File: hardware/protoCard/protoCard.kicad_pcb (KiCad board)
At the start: 2 copper layers, 100 x 99.9 mm, 2 parts, among them J1 6502 Edge, J2 6502 Pinheader

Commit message: Protoboard v0.5
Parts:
- added REF**: TestPoint_THTPad_D1.5mm_Drill0.7mm, TestPoint:TestPoint_THTPad_D1.5mm_Drill0.7mm, F.Cu at (57.4, 34.6)
- added REF**1: TestPoint_THTPad_D1.5mm_Drill0.7mm, TestPoint:TestPoint_THTPad_D1.5mm_Drill0.7mm, F.Cu at (59.9, 34.6)
- added REF**10: TestPoint_THTPad_D1.5mm_Drill0.7mm, TestPoint:TestPoint_THTPad_D1.5mm_Drill0.7mm, F.Cu at (82.8, 34.6)
- added REF**100: TestPoint_THTPad_D1.5mm_Drill0.7mm, TestPoint:TestPoint_THTPad_D1.5mm_Drill0.7mm, F.Cu at (123.4, 39.7)
- added REF**1000: TestPoint_THTPad_D1.5mm_Drill0.7mm, TestPoint:TestPoint_THTPad_D1.5mm_Drill0.7mm, F.Cu at (59.9, 103.2)
- added REF**1001: TestPoint_THTPad_D1.5mm_Drill0.7mm, TestPoint:TestPoint_THTPad_D1.5mm_Drill0.7mm, F.Cu at (62.5, 103.2)
- added REF**1002: TestPoint_THTPad_D1.5mm_Drill0.7mm, TestPoint:TestPoint_THTPad_D1.5mm_Drill0.7mm, F.Cu at (65.0, 103.2)
- added REF**1003: TestPoint_THTPad_D1.5mm_Drill0.7mm, TestPoint:TestPoint_THTPad_D1.5mm_Drill0.7mm, F.Cu at (67.6, 103.2)
- added REF**1004: TestPoint_THTPad_D1.5mm_Drill0.7mm, TestPoint:TestPoint_THTPad_D1.5mm_Drill0.7mm, F.Cu at (70.1, 103.2)
- added REF**1005: TestPoint_THTPad_D1.5mm_Drill0.7mm, TestPoint:TestPoint_THTPad_D1.5mm_Drill0.7mm, F.Cu at (72.6, 103.2)
- added REF**1006: TestPoint_THTPad_D1.5mm_Drill0.7mm, TestPoint:TestPoint_THTPad_D1.5mm_Drill0.7mm, F.Cu at (75.2, 103.2)
- added REF**1007: TestPoint_THTPad_D1.5mm_Drill0.7mm, TestPoint:TestPoint_THTPad_D1.5mm_Drill0.7mm, F.Cu at (77.7, 103.2)
- added REF**1008: TestPoint_THTPad_D1.5mm_Drill0.7mm, TestPoint:TestPoint_THTPad_D1.5mm_Drill0.7mm, F.Cu at (80.3, 103.2)
- added REF**1009: TestPoint_THTPad_D1.5mm_Drill0.7mm, TestPoint:TestPoint_THTPad_D1.5mm_Drill0.7mm, F.Cu at (82.8, 103.2)
- added REF**101: TestPoint_THTPad_D1.5mm_Drill0.7mm, TestPoint:TestPoint_THTPad_D1.5mm_Drill0.7mm, F.Cu at (126.0, 39.7)
- added REF**1010: TestPoint_THTPad_D1.5mm_Drill0.7mm, TestPoint:TestPoint_THTPad_D1.5mm_Drill0.7mm, F.Cu at (85.3, 103.2)
- added REF**1011: TestPoint_THTPad_D1.5mm_Drill0.7mm, TestPoint:TestPoint_THTPad_D1.5mm_Drill0.7mm, F.Cu at (87.9, 103.2)
- added REF**1012: TestPoint_THTPad_D1.5mm_Drill0.7mm, TestPoint:TestPoint_THTPad_D1.5mm_Drill0.7mm, F.Cu at (90.4, 103.2)
- added REF**1013: TestPoint_THTPad_D1.5mm_Drill0.7mm, TestPoint:TestPoint_THTPad_D1.5mm_Drill0.7mm, F.Cu at (93.0, 103.2)
- added REF**1014: TestPoint_THTPad_D1.5mm_Drill0.7mm, TestPoint:TestPoint_THTPad_D1.5mm_Drill0.7mm, F.Cu at (95.5, 103.2)
- added REF**1015: TestPoint_THTPad_D1.5mm_Drill0.7mm, TestPoint:TestPoint_THTPad_D1.5mm_Drill0.7mm, F.Cu at (98.0, 103.2)
- added REF**1016: TestPoint_THTPad_D1.5mm_Drill0.7mm, TestPoint:TestPoint_THTPad_D1.5mm_Drill0.7mm, F.Cu at (100.6, 103.2)
- added REF**1017: TestPoint_THTPad_D1.5mm_Drill0.7mm, TestPoint:TestPoint_THTPad_D1.5mm_Drill0.7mm, F.Cu at (103.1, 103.2)
- added REF**1018: TestPoint_THTPad_D1.5mm_Drill0.7mm, TestPoint:TestPoint_THTPad_D1.5mm_Drill0.7mm, F.Cu at (105.7, 103.2)
- added REF**1019: TestPoint_THTPad_D1.5mm_Drill0.7mm, TestPoint:TestPoint_THTPad_D1.5mm_Drill0.7mm, F.Cu at (108.2, 103.2)
- added REF**102: TestPoint_THTPad_D1.5mm_Drill0.7mm, TestPoint:TestPoint_THTPad_D1.5mm_Drill0.7mm, F.Cu at (128.5, 39.7)
- added REF**1020: TestPoint_THTPad_D1.5mm_Drill0.7mm, TestPoint:TestPoint_THTPad_D1.5mm_Drill0.7mm, F.Cu at (110.7, 103.2)
- added REF**1021: TestPoint_THTPad_D1.5mm_Drill0.7mm, TestPoint:TestPoint_THTPad_D1.5mm_Drill0.7mm, F.Cu at (113.3, 103.2)
- added REF**1022: TestPoint_THTPad_D1.5mm_Drill0.7mm, TestPoint:TestPoint_THTPad_D1.5mm_Drill0.7mm, F.Cu at (115.8, 103.2)
- added REF**1023: TestPoint_THTPad_D1.5mm_Drill0.7mm, TestPoint:TestPoint_THTPad_D1.5mm_Drill0.7mm, F.Cu at (118.4, 103.2)
- added REF**1024: TestPoint_THTPad_D1.5mm_Drill0.7mm, TestPoint:TestPoint_THTPad_D1.5mm_Drill0.7mm, F.Cu at (120.9, 103.2)
- added REF**1025: TestPoint_THTPad_D1.5mm_Drill0.7mm, TestPoint:TestPoint_THTPad_D1.5mm_Drill0.7mm, F.Cu at (123.4, 103.2)
- added REF**1026: TestPoint_THTPad_D1.5mm_Drill0.7mm, TestPoint:TestPoint_THTPad_D1.5mm_Drill0.7mm, F.Cu at (126.0, 103.2)
- added REF**1027: TestPoint_THTPad_D1.5mm_Drill0.7mm, TestPoint:TestPoint_THTPad_D1.5mm_Drill0.7mm, F.Cu at (128.5, 103.2)
- added REF**1028: TestPoint_THTPad_D1.5mm_Drill0.7mm, TestPoint:TestPoint_THTPad_D1.5mm_Drill0.7mm, F.Cu at (131.1, 103.2)
- added REF**1029: TestPoint_THTPad_D1.5mm_Drill0.7mm, TestPoint:TestPoint_THTPad_D1.5mm_Drill0.7mm, F.Cu at (133.6, 103.2)
- added REF**103: TestPoint_THTPad_D1.5mm_Drill0.7mm, TestPoint:TestPoint_THTPad_D1.5mm_Drill0.7mm, F.Cu at (131.1, 39.7)
- added REF**1030: TestPoint_THTPad_D1.5mm_Drill0.7mm, TestPoint:TestPoint_THTPad_D1.5mm_Drill0.7mm, F.Cu at (136.1, 103.2)
- added REF**1031: TestPoint_THTPad_D1.5mm_Drill0.7mm, TestPoint:TestPoint_THTPad_D1.5mm_Drill0.7mm, F.Cu at (138.7, 103.2)
- added REF**1032: TestPoint_THTPad_D1.5mm_Drill0.7mm, TestPoint:TestPoint_THTPad_D1.5mm_Drill0.7mm, F.Cu at (141.2, 103.2)
- added REF**1033: TestPoint_THTPad_D1.5mm_Drill0.7mm, TestPoint:TestPoint_THTPad_D1.5mm_Drill0.7mm, F.Cu at (143.8, 103.2)
- added REF**1034: TestPoint_THTPad_D1.5mm_Drill0.7mm, TestPoint:TestPoint_THTPad_D1.5mm_Drill0.7mm, F.Cu at (146.3, 103.2)
- added REF**1035: TestPoint_THTPad_D1.5mm_Drill0.7mm, TestPoint:TestPoint_THTPad_D1.5mm_Drill0.7mm, F.Cu at (148.8, 103.2)
- added REF**1037: TestPoint_THTPad_D1.5mm_Drill0.7mm, TestPoint:TestPoint_THTPad_D1.5mm_Drill0.7mm, F.Cu at (59.9, 105.7)
- added REF**1038: TestPoint_THTPad_D1.5mm_Drill0.7mm, TestPoint:TestPoint_THTPad_D1.5mm_Drill0.7mm, F.Cu at (62.5, 105.7)
- added REF**1039: TestPoint_THTPad_D1.5mm_Drill0.7mm, TestPoint:TestPoint_THTPad_D1.5mm_Drill0.7mm, F.Cu at (65.0, 105.7)
- added REF**104: TestPoint_THTPad_D1.5mm_Drill0.7mm, TestPoint:TestPoint_THTPad_D1.5mm_Drill0.7mm, F.Cu at (133.6, 39.7)
- added REF**1040: TestPoint_THTPad_D1.5mm_Drill0.7mm, TestPoint:TestPoint_THTPad_D1.5mm_Drill0.7mm, F.Cu at (67.6, 105.7)
- added REF**1041: TestPoint_THTPad_D1.5mm_Drill0.7mm, TestPoint:TestPoint_THTPad_D1.5mm_Drill0.7mm, F.Cu at (70.1, 105.7)
- added REF**1042: TestPoint_THTPad_D1.5mm_Drill0.7mm, TestPoint:TestPoint_THTPad_D1.5mm_Drill0.7mm, F.Cu at (72.6, 105.7)
- added REF**1043: TestPoint_THTPad_D1.5mm_Drill0.7mm, TestPoint:TestPoint_THTPad_D1.5mm_Drill0.7mm, F.Cu at (75.2, 105.7)
- added REF**1044: TestPoint_THTPad_D1.5mm_Drill0.7mm, TestPoint:TestPoint_THTPad_D1.5mm_Drill0.7mm, F.Cu at (77.7, 105.7)
- added REF**1045: TestPoint_THTPad_D1.5mm_Drill0.7mm, TestPoint:TestPoint_THTPad_D1.5mm_Drill0.7mm, F.Cu at (80.3, 105.7)
- added REF**1046: TestPoint_THTPad_D1.5mm_Drill0.7mm, TestPoint:TestPoint_THTPad_D1.5mm_Drill0.7mm, F.Cu at (82.8, 105.7)
- added REF**1047: TestPoint_THTPad_D1.5mm_Drill0.7mm, TestPoint:TestPoint_THTPad_D1.5mm_Drill0.7mm, F.Cu at (85.3, 105.7)
- added REF**1048: TestPoint_THTPad_D1.5mm_Drill0.7mm, TestPoint:TestPoint_THTPad_D1.5mm_Drill0.7mm, F.Cu at (87.9, 105.7)
- added REF**1049: TestPoint_THTPad_D1.5mm_Drill0.7mm, TestPoint:TestPoint_THTPad_D1.5mm_Drill0.7mm, F.Cu at (90.4, 105.7)
- added REF**105: TestPoint_THTPad_D1.5mm_Drill0.7mm, TestPoint:TestPoint_THTPad_D1.5mm_Drill0.7mm, F.Cu at (136.1, 39.7)
- added REF**1050: TestPoint_THTPad_D1.5mm_Drill0.7mm, TestPoint:TestPoint_THTPad_D1.5mm_Drill0.7mm, F.Cu at (93.0, 105.7)
- added REF**1051: TestPoint_THTPad_D1.5mm_Drill0.7mm, TestPoint:TestPoint_THTPad_D1.5mm_Drill0.7mm, F.Cu at (95.5, 105.7)
- added REF**1052: TestPoint_THTPad_D1.5mm_Drill0.7mm, TestPoint:TestPoint_THTPad_D1.5mm_Drill0.7mm, F.Cu at (98.0, 105.7)
- added REF**1053: TestPoint_THTPad_D1.5mm_Drill0.7mm, TestPoint:TestPoint_THTPad_D1.5mm_Drill0.7mm, F.Cu at (100.6, 105.7)
- added REF**1054: TestPoint_THTPad_D1.5mm_Drill0.7mm, TestPoint:TestPoint_THTPad_D1.5mm_Drill0.7mm, F.Cu at (103.1, 105.7)
- added REF**1055: TestPoint_THTPad_D1.5mm_Drill0.7mm, TestPoint:TestPoint_THTPad_D1.5mm_Drill0.7mm, F.Cu at (105.7, 105.7)
- added REF**1056: TestPoint_THTPad_D1.5mm_Drill0.7mm, TestPoint:TestPoint_THTPad_D1.5mm_Drill0.7mm, F.Cu at (108.2, 105.7)
- added REF**1057: TestPoint_THTPad_D1.5mm_Drill0.7mm, TestPoint:TestPoint_THTPad_D1.5mm_Drill0.7mm, F.Cu at (110.7, 105.7)
- added REF**1058: TestPoint_THTPad_D1.5mm_Drill0.7mm, TestPoint:TestPoint_THTPad_D1.5mm_Drill0.7mm, F.Cu at (113.3, 105.7)
- added REF**1059: TestPoint_THTPad_D1.5mm_Drill0.7mm, TestPoint:TestPoint_THTPad_D1.5mm_Drill0.7mm, F.Cu at (115.8, 105.7)
- added REF**106: TestPoint_THTPad_D1.5mm_Drill0.7mm, TestPoint:TestPoint_THTPad_D1.5mm_Drill0.7mm, F.Cu at (138.7, 39.7)
- added REF**1060: TestPoint_THTPad_D1.5mm_Drill0.7mm, TestPoint:TestPoint_THTPad_D1.5mm_Drill0.7mm, F.Cu at (118.4, 105.7)
- added REF**1061: TestPoint_THTPad_D1.5mm_Drill0.7mm, TestPoint:TestPoint_THTPad_D1.5mm_Drill0.7mm, F.Cu at (120.9, 105.7)
- added REF**1062: TestPoint_THTPad_D1.5mm_Drill0.7mm, TestPoint:TestPoint_THTPad_D1.5mm_Drill0.7mm, F.Cu at (123.4, 105.7)
- added REF**1063: TestPoint_THTPad_D1.5mm_Drill0.7mm, TestPoint:TestPoint_THTPad_D1.5mm_Drill0.7mm, F.Cu at (126.0, 105.7)
- added REF**1064: TestPoint_THTPad_D1.5mm_Drill0.7mm, TestPoint:TestPoint_THTPad_D1.5mm_Drill0.7mm, F.Cu at (128.5, 105.7)
- added REF**1065: TestPoint_THTPad_D1.5mm_Drill0.7mm, TestPoint:TestPoint_THTPad_D1.5mm_Drill0.7mm, F.Cu at (131.1, 105.7)
- added REF**1066: TestPoint_THTPad_D1.5mm_Drill0.7mm, TestPoint:TestPoint_THTPad_D1.5mm_Drill0.7mm, F.Cu at (133.6, 105.7)
- added REF**1067: TestPoint_THTPad_D1.5mm_Drill0.7mm, TestPoint:TestPoint_THTPad_D1.5mm_Drill0.7mm, F.Cu at (136.1, 105.7)
- added REF**1068: TestPoint_THTPad_D1.5mm_Drill0.7mm, TestPoint:TestPoint_THTPad_D1.5mm_Drill0.7mm, F.Cu at (138.7, 105.7)
- added REF**1069: TestPoint_THTPad_D1.5mm_Drill0.7mm, TestPoint:TestPoint_THTPad_D1.5mm_Drill0.7mm, F.Cu at (141.2, 105.7)
- added REF**107: TestPoint_THTPad_D1.5mm_Drill0.7mm, TestPoint:TestPoint_THTPad_D1.5mm_Drill0.7mm, F.Cu at (141.2, 39.7)
- added REF**1070: TestPoint_THTPad_D1.5mm_Drill0.7mm, TestPoint:TestPoint_THTPad_D1.5mm_Drill0.7mm, F.Cu at (143.8, 105.7)
- added REF**1071: TestPoint_THTPad_D1.5mm_Drill0.7mm, TestPoint:TestPoint_THTPad_D1.5mm_Drill0.7mm, F.Cu at (146.3, 105.7)
- added REF**1072: TestPoint_THTPad_D1.5mm_Drill0.7mm, TestPoint:TestPoint_THTPad_D1.5mm_Drill0.7mm, F.Cu at (148.8, 105.7)
- added REF**108: TestPoint_THTPad_D1.5mm_Drill0.7mm, TestPoint:TestPoint_THTPad_D1.5mm_Drill0.7mm, F.Cu at (143.8, 39.7)
- added REF**109: TestPoint_THTPad_D1.5mm_Drill0.7mm, TestPoint:TestPoint_THTPad_D1.5mm_Drill0.7mm, F.Cu at (148.8, 39.7)
- added REF**11: TestPoint_THTPad_D1.5mm_Drill0.7mm, TestPoint:TestPoint_THTPad_D1.5mm_Drill0.7mm, F.Cu at (85.3, 34.6)
- added REF**110: TestPoint_THTPad_D1.5mm_Drill0.7mm, TestPoint:TestPoint_THTPad_D1.5mm_Drill0.7mm, F.Cu at (148.8, 42.2)
- added REF**111: TestPoint_THTPad_D1.5mm_Drill0.7mm, TestPoint:TestPoint_THTPad_D1.5mm_Drill0.7mm, F.Cu at (57.4, 42.2)
- added REF**112: TestPoint_THTPad_D1.5mm_Drill0.7mm, TestPoint:TestPoint_THTPad_D1.5mm_Drill0.7mm, F.Cu at (59.9, 42.2)
- added REF**113: TestPoint_THTPad_D1.5mm_Drill0.7mm, TestPoint:TestPoint_THTPad_D1.5mm_Drill0.7mm, F.Cu at (62.5, 42.2)
- added REF**114: TestPoint_THTPad_D1.5mm_Drill0.7mm, TestPoint:TestPoint_THTPad_D1.5mm_Drill0.7mm, F.Cu at (65.0, 42.2)
- added REF**115: TestPoint_THTPad_D1.5mm_Drill0.7mm, TestPoint:TestPoint_THTPad_D1.5mm_Drill0.7mm, F.Cu at (67.6, 42.2)
- added REF**116: TestPoint_THTPad_D1.5mm_Drill0.7mm, TestPoint:TestPoint_THTPad_D1.5mm_Drill0.7mm, F.Cu at (70.1, 42.2)
- added REF**117: TestPoint_THTPad_D1.5mm_Drill0.7mm, TestPoint:TestPoint_THTPad_D1.5mm_Drill0.7mm, F.Cu at (72.6, 42.2)
- added REF**118: TestPoint_THTPad_D1.5mm_Drill0.7mm, TestPoint:TestPoint_THTPad_D1.5mm_Drill0.7mm, F.Cu at (75.2, 42.2)
- added REF**119: TestPoint_THTPad_D1.5mm_Drill0.7mm, TestPoint:TestPoint_THTPad_D1.5mm_Drill0.7mm, F.Cu at (77.7, 42.2)
- added REF**12: TestPoint_THTPad_D1.5mm_Drill0.7mm, TestPoint:TestPoint_THTPad_D1.5mm_Drill0.7mm, F.Cu at (87.9, 34.6)
- added REF**120: TestPoint_THTPad_D1.5mm_Drill0.7mm, TestPoint:TestPoint_THTPad_D1.5mm_Drill0.7mm, F.Cu at (80.3, 42.2)
- added REF**121: TestPoint_THTPad_D1.5mm_Drill0.7mm, TestPoint:TestPoint_THTPad_D1.5mm_Drill0.7mm, F.Cu at (82.8, 42.2)
- added REF**122: TestPoint_THTPad_D1.5mm_Drill0.7mm, TestPoint:TestPoint_THTPad_D1.5mm_Drill0.7mm, F.Cu at (85.3, 42.2)
- added REF**123: TestPoint_THTPad_D1.5mm_Drill0.7mm, TestPoint:TestPoint_THTPad_D1.5mm_Drill0.7mm, F.Cu at (87.9, 42.2)
- added REF**124: TestPoint_THTPad_D1.5mm_Drill0.7mm, TestPoint:TestPoint_THTPad_D1.5mm_Drill0.7mm, F.Cu at (90.4, 42.2)
- added REF**125: TestPoint_THTPad_D1.5mm_Drill0.7mm, TestPoint:TestPoint_THTPad_D1.5mm_Drill0.7mm, F.Cu at (93.0, 42.2)
- added REF**126: TestPoint_THTPad_D1.5mm_Drill0.7mm, TestPoint:TestPoint_THTPad_D1.5mm_Drill0.7mm, F.Cu at (95.5, 42.2)
- added REF**127: TestPoint_THTPad_D1.5mm_Drill0.7mm, TestPoint:TestPoint_THTPad_D1.5mm_Drill0.7mm, F.Cu at (98.0, 42.2)
- added REF**128: TestPoint_THTPad_D1.5mm_Drill0.7mm, TestPoint:TestPoint_THTPad_D1.5mm_Drill0.7mm, F.Cu at (100.6, 42.2)
- added REF**129: TestPoint_THTPad_D1.5mm_Drill0.7mm, TestPoint:TestPoint_THTPad_D1.5mm_Drill0.7mm, F.Cu at (103.1, 42.2)
- added REF**13: TestPoint_THTPad_D1.5mm_Drill0.7mm, TestPoint:TestPoint_THTPad_D1.5mm_Drill0.7mm, F.Cu at (90.4, 34.6)
- added REF**130: TestPoint_THTPad_D1.5mm_Drill0.7mm, TestPoint:TestPoint_THTPad_D1.5mm_Drill0.7mm, F.Cu at (105.7, 42.2)
- added REF**131: TestPoint_THTPad_D1.5mm_Drill0.7mm, TestPoint:TestPoint_THTPad_D1.5mm_Drill0.7mm, F.Cu at (108.2, 42.2)
- added REF**132: TestPoint_THTPad_D1.5mm_Drill0.7mm, TestPoint:TestPoint_THTPad_D1.5mm_Drill0.7mm, F.Cu at (110.7, 42.2)
- added REF**133: TestPoint_THTPad_D1.5mm_Drill0.7mm, TestPoint:TestPoint_THTPad_D1.5mm_Drill0.7mm, F.Cu at (113.3, 42.2)
- added REF**134: TestPoint_THTPad_D1.5mm_Drill0.7mm, TestPoint:TestPoint_THTPad_D1.5mm_Drill0.7mm, F.Cu at (115.8, 42.2)
- added REF**135: TestPoint_THTPad_D1.5mm_Drill0.7mm, TestPoint:TestPoint_THTPad_D1.5mm_Drill0.7mm, F.Cu at (118.4, 42.2)
- added REF**136: TestPoint_THTPad_D1.5mm_Drill0.7mm, TestPoint:TestPoint_THTPad_D1.5mm_Drill0.7mm, F.Cu at (120.9, 42.2)
- added REF**137: TestPoint_THTPad_D1.5mm_Drill0.7mm, TestPoint:TestPoint_THTPad_D1.5mm_Drill0.7mm, F.Cu at (123.4, 42.2)
- added REF**138: TestPoint_THTPad_D1.5mm_Drill0.7mm, TestPoint:TestPoint_THTPad_D1.5mm_Drill0.7mm, F.Cu at (126.0, 42.2)
- added REF**139: TestPoint_THTPad_D1.5mm_Drill0.7mm, TestPoint:TestPoint_THTPad_D1.5mm_Drill0.7mm, F.Cu at (128.5, 42.2)
- added REF**14: TestPoint_THTPad_D1.5mm_Drill0.7mm, TestPoint:TestPoint_THTPad_D1.5mm_Drill0.7mm, F.Cu at (93.0, 34.6)
- added REF**140: TestPoint_THTPad_D1.5mm_Drill0.7mm, TestPoint:TestPoint_THTPad_D1.5mm_Drill0.7mm, F.Cu at (131.1, 42.2)
- added REF**141: TestPoint_THTPad_D1.5mm_Drill0.7mm, TestPoint:TestPoint_THTPad_D1.5mm_Drill0.7mm, F.Cu at (133.6, 42.2)
- added REF**142: TestPoint_THTPad_D1.5mm_Drill0.7mm, TestPoint:TestPoint_THTPad_D1.5mm_Drill0.7mm, F.Cu at (136.1, 42.2)
- added REF**143: TestPoint_THTPad_D1.5mm_Drill0.7mm, TestPoint:TestPoint_THTPad_D1.5mm_Drill0.7mm, F.Cu at (138.7, 42.2)
- added REF**144: TestPoint_THTPad_D1.5mm_Drill0.7mm, TestPoint:TestPoint_THTPad_D1.5mm_Drill0.7mm, F.Cu at (141.2, 42.2)
- added REF**145: TestPoint_THTPad_D1.5mm_Drill0.7mm, TestPoint:TestPoint_THTPad_D1.5mm_Drill0.7mm, F.Cu at (143.8, 42.2)
- added REF**146: TestPoint_THTPad_D1.5mm_Drill0.7mm, TestPoint:TestPoint_THTPad_D1.5mm_Drill0.7mm, F.Cu at (148.8, 44.8)
- added REF**147: TestPoint_THTPad_D1.5mm_Drill0.7mm, TestPoint:TestPoint_THTPad_D1.5mm_Drill0.7mm, F.Cu at (148.8, 47.3)
- added REF**148: TestPoint_THTPad_D1.5mm_Drill0.7mm, TestPoint:TestPoint_THTPad_D1.5mm_Drill0.7mm, F.Cu at (57.4, 44.8)
- added REF**149: TestPoint_THTPad_D1.5mm_Drill0.7mm, TestPoint:TestPoint_THTPad_D1.5mm_Drill0.7mm, F.Cu at (59.9, 44.8)
- added REF**15: TestPoint_THTPad_D1.5mm_Drill0.7mm, TestPoint:TestPoint_THTPad_D1.5mm_Drill0.7mm, F.Cu at (95.5, 34.6)
- added REF**150: TestPoint_THTPad_D1.5mm_Drill0.7mm, TestPoint:TestPoint_THTPad_D1.5mm_Drill0.7mm, F.Cu at (62.5, 44.8)
- added REF**151: TestPoint_THTPad_D1.5mm_Drill0.7mm, TestPoint:TestPoint_THTPad_D1.5mm_Drill0.7mm, F.Cu at (65.0, 44.8)
- added REF**152: TestPoint_THTPad_D1.5mm_Drill0.7mm, TestPoint:TestPoint_THTPad_D1.5mm_Drill0.7mm, F.Cu at (67.6, 44.8)
- added REF**153: TestPoint_THTPad_D1.5mm_Drill0.7mm, TestPoint:TestPoint_THTPad_D1.5mm_Drill0.7mm, F.Cu at (70.1, 44.8)
- added REF**154: TestPoint_THTPad_D1.5mm_Drill0.7mm, TestPoint:TestPoint_THTPad_D1.5mm_Drill0.7mm, F.Cu at (72.6, 44.8)
- added REF**155: TestPoint_THTPad_D1.5mm_Drill0.7mm, TestPoint:TestPoint_THTPad_D1.5mm_Drill0.7mm, F.Cu at (75.2, 44.8)
- added REF**156: TestPoint_THTPad_D1.5mm_Drill0.7mm, TestPoint:TestPoint_THTPad_D1.5mm_Drill0.7mm, F.Cu at (77.7, 44.8)
- added REF**157: TestPoint_THTPad_D1.5mm_Drill0.7mm, TestPoint:TestPoint_THTPad_D1.5mm_Drill0.7mm, F.Cu at (80.3, 44.8)
- added REF**158: TestPoint_THTPad_D1.5mm_Drill0.7mm, TestPoint:TestPoint_THTPad_D1.5mm_Drill0.7mm, F.Cu at (82.8, 44.8)
- added REF**159: TestPoint_THTPad_D1.5mm_Drill0.7mm, TestPoint:TestPoint_THTPad_D1.5mm_Drill0.7mm, F.Cu at (85.3, 44.8)
- added REF**16: TestPoint_THTPad_D1.5mm_Drill0.7mm, TestPoint:TestPoint_THTPad_D1.5mm_Drill0.7mm, F.Cu at (98.0, 34.6)
- added REF**160: TestPoint_THTPad_D1.5mm_Drill0.7mm, TestPoint:TestPoint_THTPad_D1.5mm_Drill0.7mm, F.Cu at (87.9, 44.8)
- added REF**161: TestPoint_THTPad_D1.5mm_Drill0.7mm, TestPoint:TestPoint_THTPad_D1.5mm_Drill0.7mm, F.Cu at (90.4, 44.8)
- added REF**162: TestPoint_THTPad_D1.5mm_Drill0.7mm, TestPoint:TestPoint_THTPad_D1.5mm_Drill0.7mm, F.Cu at (93.0, 44.8)
- added REF**163: TestPoint_THTPad_D1.5mm_Drill0.7mm, TestPoint:TestPoint_THTPad_D1.5mm_Drill0.7mm, F.Cu at (95.5, 44.8)
- added REF**164: TestPoint_THTPad_D1.5mm_Drill0.7mm, TestPoint:TestPoint_THTPad_D1.5mm_Drill0.7mm, F.Cu at (98.0, 44.8)
- added REF**165: TestPoint_THTPad_D1.5mm_Drill0.7mm, TestPoint:TestPoint_THTPad_D1.5mm_Drill0.7mm, F.Cu at (100.6, 44.8)
- added REF**166: TestPoint_THTPad_D1.5mm_Drill0.7mm, TestPoint:TestPoint_THTPad_D1.5mm_Drill0.7mm, F.Cu at (103.1, 44.8)
- added REF**167: TestPoint_THTPad_D1.5mm_Drill0.7mm, TestPoint:TestPoint_THTPad_D1.5mm_Drill0.7mm, F.Cu at (105.7, 44.8)
- added REF**168: TestPoint_THTPad_D1.5mm_Drill0.7mm, TestPoint:TestPoint_THTPad_D1.5mm_Drill0.7mm, F.Cu at (108.2, 44.8)
- added REF**169: TestPoint_THTPad_D1.5mm_Drill0.7mm, TestPoint:TestPoint_THTPad_D1.5mm_Drill0.7mm, F.Cu at (110.7, 44.8)
- added REF**17: TestPoint_THTPad_D1.5mm_Drill0.7mm, TestPoint:TestPoint_THTPad_D1.5mm_Drill0.7mm, F.Cu at (100.6, 34.6)
- added REF**170: TestPoint_THTPad_D1.5mm_Drill0.7mm, TestPoint:TestPoint_THTPad_D1.5mm_Drill0.7mm, F.Cu at (113.3, 44.8)
- added REF**171: TestPoint_THTPad_D1.5mm_Drill0.7mm, TestPoint:TestPoint_THTPad_D1.5mm_Drill0.7mm, F.Cu at (115.8, 44.8)
- added REF**172: TestPoint_THTPad_D1.5mm_Drill0.7mm, TestPoint:TestPoint_THTPad_D1.5mm_Drill0.7mm, F.Cu at (118.4, 44.8)
- added REF**173: TestPoint_THTPad_D1.5mm_Drill0.7mm, TestPoint:TestPoint_THTPad_D1.5mm_Drill0.7mm, F.Cu at (120.9, 44.8)
- added REF**174: TestPoint_THTPad_D1.5mm_Drill0.7mm, TestPoint:TestPoint_THTPad_D1.5mm_Drill0.7mm, F.Cu at (123.4, 44.8)
- added REF**175: TestPoint_THTPad_D1.5mm_Drill0.7mm, TestPoint:TestPoint_THTPad_D1.5mm_Drill0.7mm, F.Cu at (126.0, 44.8)
- added REF**176: TestPoint_THTPad_D1.5mm_Drill0.7mm, TestPoint:TestPoint_THTPad_D1.5mm_Drill0.7mm, F.Cu at (128.5, 44.8)
- added REF**177: TestPoint_THTPad_D1.5mm_Drill0.7mm, TestPoint:TestPoint_THTPad_D1.5mm_Drill0.7mm, F.Cu at (131.1, 44.8)
- added REF**178: TestPoint_THTPad_D1.5mm_Drill0.7mm, TestPoint:TestPoint_THTPad_D1.5mm_Drill0.7mm, F.Cu at (133.6, 44.8)
- added REF**179: TestPoint_THTPad_D1.5mm_Drill0.7mm, TestPoint:TestPoint_THTPad_D1.5mm_Drill0.7mm, F.Cu at (136.1, 44.8)
- added REF**18: TestPoint_THTPad_D1.5mm_Drill0.7mm, TestPoint:TestPoint_THTPad_D1.5mm_Drill0.7mm, F.Cu at (103.1, 34.6)
- added REF**180: TestPoint_THTPad_D1.5mm_Drill0.7mm, TestPoint:TestPoint_THTPad_D1.5mm_Drill0.7mm, F.Cu at (138.7, 44.8)
- added REF**181: TestPoint_THTPad_D1.5mm_Drill0.7mm, TestPoint:TestPoint_THTPad_D1.5mm_Drill0.7mm, F.Cu at (141.2, 44.8)
- added REF**182: TestPoint_THTPad_D1.5mm_Drill0.7mm, TestPoint:TestPoint_THTPad_D1.5mm_Drill0.7mm, F.Cu at (143.8, 44.8)
- added REF**183: TestPoint_THTPad_D1.5mm_Drill0.7mm, TestPoint:TestPoint_THTPad_D1.5mm_Drill0.7mm, F.Cu at (148.8, 49.8)
- added REF**184: TestPoint_THTPad_D1.5mm_Drill0.7mm, TestPoint:TestPoint_THTPad_D1.5mm_Drill0.7mm, F.Cu at (148.8, 52.4)
- added REF**185: TestPoint_THTPad_D1.5mm_Drill0.7mm, TestPoint:TestPoint_THTPad_D1.5mm_Drill0.7mm, F.Cu at (57.4, 47.3)
- added REF**186: TestPoint_THTPad_D1.5mm_Drill0.7mm, TestPoint:TestPoint_THTPad_D1.5mm_Drill0.7mm, F.Cu at (59.9, 47.3)
- added REF**187: TestPoint_THTPad_D1.5mm_Drill0.7mm, TestPoint:TestPoint_THTPad_D1.5mm_Drill0.7mm, F.Cu at (62.5, 47.3)
- added REF**188: TestPoint_THTPad_D1.5mm_Drill0.7mm, TestPoint:TestPoint_THTPad_D1.5mm_Drill0.7mm, F.Cu at (65.0, 47.3)
- added REF**189: TestPoint_THTPad_D1.5mm_Drill0.7mm, TestPoint:TestPoint_THTPad_D1.5mm_Drill0.7mm, F.Cu at (67.6, 47.3)
- added REF**19: TestPoint_THTPad_D1.5mm_Drill0.7mm, TestPoint:TestPoint_THTPad_D1.5mm_Drill0.7mm, F.Cu at (105.7, 34.6)
- added REF**190: TestPoint_THTPad_D1.5mm_Drill0.7mm, TestPoint:TestPoint_THTPad_D1.5mm_Drill0.7mm, F.Cu at (70.1, 47.3)
- added REF**191: TestPoint_THTPad_D1.5mm_Drill0.7mm, TestPoint:TestPoint_THTPad_D1.5mm_Drill0.7mm, F.Cu at (72.6, 47.3)
- added REF**192: TestPoint_THTPad_D1.5mm_Drill0.7mm, TestPoint:TestPoint_THTPad_D1.5mm_Drill0.7mm, F.Cu at (75.2, 47.3)
- added REF**193: TestPoint_THTPad_D1.5mm_Drill0.7mm, TestPoint:TestPoint_THTPad_D1.5mm_Drill0.7mm, F.Cu at (77.7, 47.3)
- added REF**194: TestPoint_THTPad_D1.5mm_Drill0.7mm, TestPoint:TestPoint_THTPad_D1.5mm_Drill0.7mm, F.Cu at (80.3, 47.3)
- added REF**195: TestPoint_THTPad_D1.5mm_Drill0.7mm, TestPoint:TestPoint_THTPad_D1.5mm_Drill0.7mm, F.Cu at (82.8, 47.3)
- added REF**196: TestPoint_THTPad_D1.5mm_Drill0.7mm, TestPoint:TestPoint_THTPad_D1.5mm_Drill0.7mm, F.Cu at (85.3, 47.3)
- added REF**197: TestPoint_THTPad_D1.5mm_Drill0.7mm, TestPoint:TestPoint_THTPad_D1.5mm_Drill0.7mm, F.Cu at (87.9, 47.3)
- added REF**198: TestPoint_THTPad_D1.5mm_Drill0.7mm, TestPoint:TestPoint_THTPad_D1.5mm_Drill0.7mm, F.Cu at (90.4, 47.3)
- added REF**199: TestPoint_THTPad_D1.5mm_Drill0.7mm, TestPoint:TestPoint_THTPad_D1.5mm_Drill0.7mm, F.Cu at (93.0, 47.3)
- added REF**2: TestPoint_THTPad_D1.5mm_Drill0.7mm, TestPoint:TestPoint_THTPad_D1.5mm_Drill0.7mm, F.Cu at (62.5, 34.6)
- added REF**20: TestPoint_THTPad_D1.5mm_Drill0.7mm, TestPoint:TestPoint_THTPad_D1.5mm_Drill0.7mm, F.Cu at (108.2, 34.6)
- added REF**200: TestPoint_THTPad_D1.5mm_Drill0.7mm, TestPoint:TestPoint_THTPad_D1.5mm_Drill0.7mm, F.Cu at (95.5, 47.3)
- added REF**201: TestPoint_THTPad_D1.5mm_Drill0.7mm, TestPoint:TestPoint_THTPad_D1.5mm_Drill0.7mm, F.Cu at (98.0, 47.3)
- added REF**202: TestPoint_THTPad_D1.5mm_Drill0.7mm, TestPoint:TestPoint_THTPad_D1.5mm_Drill0.7mm, F.Cu at (100.6, 47.3)
- added REF**203: TestPoint_THTPad_D1.5mm_Drill0.7mm, TestPoint:TestPoint_THTPad_D1.5mm_Drill0.7mm, F.Cu at (103.1, 47.3)
- added REF**204: TestPoint_THTPad_D1.5mm_Drill0.7mm, TestPoint:TestPoint_THTPad_D1.5mm_Drill0.7mm, F.Cu at (105.7, 47.3)
- added REF**205: TestPoint_THTPad_D1.5mm_Drill0.7mm, TestPoint:TestPoint_THTPad_D1.5mm_Drill0.7mm, F.Cu at (108.2, 47.3)
- added REF**206: TestPoint_THTPad_D1.5mm_Drill0.7mm, TestPoint:TestPoint_THTPad_D1.5mm_Drill0.7mm, F.Cu at (110.7, 47.3)
- added REF**207: TestPoint_THTPad_D1.5mm_Drill0.7mm, TestPoint:TestPoint_THTPad_D1.5mm_Drill0.7mm, F.Cu at (113.3, 47.3)
- added REF**208: TestPoint_THTPad_D1.5mm_Drill0.7mm, TestPoint:TestPoint_THTPad_D1.5mm_Drill0.7mm, F.Cu at (115.8, 47.3)
- added REF**209: TestPoint_THTPad_D1.5mm_Drill0.7mm, TestPoint:TestPoint_THTPad_D1.5mm_Drill0.7mm, F.Cu at (118.4, 47.3)
- added REF**21: TestPoint_THTPad_D1.5mm_Drill0.7mm, TestPoint:TestPoint_THTPad_D1.5mm_Drill0.7mm, F.Cu at (110.7, 34.6)
- added REF**210: TestPoint_THTPad_D1.5mm_Drill0.7mm, TestPoint:TestPoint_THTPad_D1.5mm_Drill0.7mm, F.Cu at (120.9, 47.3)
- added REF**211: TestPoint_THTPad_D1.5mm_Drill0.7mm, TestPoint:TestPoint_THTPad_D1.5mm_Drill0.7mm, F.Cu at (123.4, 47.3)
- added REF**212: TestPoint_THTPad_D1.5mm_Drill0.7mm, TestPoint:TestPoint_THTPad_D1.5mm_Drill0.7mm, F.Cu at (126.0, 47.3)
- added REF**213: TestPoint_THTPad_D1.5mm_Drill0.7mm, TestPoint:TestPoint_THTPad_D1.5mm_Drill0.7mm, F.Cu at (128.5, 47.3)
- added REF**214: TestPoint_THTPad_D1.5mm_Drill0.7mm, TestPoint:TestPoint_THTPad_D1.5mm_Drill0.7mm, F.Cu at (131.1, 47.3)
- added REF**215: TestPoint_THTPad_D1.5mm_Drill0.7mm, TestPoint:TestPoint_THTPad_D1.5mm_Drill0.7mm, F.Cu at (133.6, 47.3)
- added REF**216: TestPoint_THTPad_D1.5mm_Drill0.7mm, TestPoint:TestPoint_THTPad_D1.5mm_Drill0.7mm, F.Cu at (136.1, 47.3)
- added REF**217: TestPoint_THTPad_D1.5mm_Drill0.7mm, TestPoint:TestPoint_THTPad_D1.5mm_Drill0.7mm, F.Cu at (138.7, 47.3)
- added REF**218: TestPoint_THTPad_D1.5mm_Drill0.7mm, TestPoint:TestPoint_THTPad_D1.5mm_Drill0.7mm, F.Cu at (141.2, 47.3)
- added REF**219: TestPoint_THTPad_D1.5mm_Drill0.7mm, TestPoint:TestPoint_THTPad_D1.5mm_Drill0.7mm, F.Cu at (143.8, 47.3)
- added REF**22: TestPoint_THTPad_D1.5mm_Drill0.7mm, TestPoint:TestPoint_THTPad_D1.5mm_Drill0.7mm, F.Cu at (113.3, 34.6)
- added REF**220: TestPoint_THTPad_D1.5mm_Drill0.7mm, TestPoint:TestPoint_THTPad_D1.5mm_Drill0.7mm, F.Cu at (148.8, 54.9)
- added REF**221: TestPoint_THTPad_D1.5mm_Drill0.7mm, TestPoint:TestPoint_THTPad_D1.5mm_Drill0.7mm, F.Cu at (148.8, 57.5)
- added REF**222: TestPoint_THTPad_D1.5mm_Drill0.7mm, TestPoint:TestPoint_THTPad_D1.5mm_Drill0.7mm, F.Cu at (57.4, 49.8)
- added REF**223: TestPoint_THTPad_D1.5mm_Drill0.7mm, TestPoint:TestPoint_THTPad_D1.5mm_Drill0.7mm, F.Cu at (59.9, 49.8)
- added REF**224: TestPoint_THTPad_D1.5mm_Drill0.7mm, TestPoint:TestPoint_THTPad_D1.5mm_Drill0.7mm, F.Cu at (62.5, 49.8)
- added REF**225: TestPoint_THTPad_D1.5mm_Drill0.7mm, TestPoint:TestPoint_THTPad_D1.5mm_Drill0.7mm, F.Cu at (65.0, 49.8)
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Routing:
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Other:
- board text added: "A0 A1 A2 A3 A4 A5 A6 A7"
- board text added: "Protoboard"
- board text added: "VCC"

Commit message: Protoboard v1.0
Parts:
- removed REF**1071, REF**1072, REF**553, REF**962, REF**963, REF**964, REF**965, REF**966, REF**967, REF**968, REF**969, REF**970, REF**971, REF**972, REF**973, REF**974, REF**975, REF**976, REF**977, REF**978, REF**979, REF**980, REF**981, REF**982, REF**983, REF**984, REF**985, REF**986, REF**987, REF**988, REF**989, REF**990, REF**991, REF**992, REF**993, REF**994, REF**995, REF**996, REF**998: TestPoint_THTPad_D1.5mm_Drill0.7mm, TestPoint:TestPoint_THTPad_D1.5mm_Drill0.7mm
- moved REF**1000 2.23 mm to (59.9, 101.0)
- moved REF**1001 2.23 mm to (62.5, 101.0)
- moved REF**1002 2.23 mm to (65.0, 101.0)
- moved REF**1003 2.23 mm to (67.6, 101.0)
- moved REF**1004 2.23 mm to (70.1, 101.0)
- moved REF**1005 2.23 mm to (72.6, 101.0)
- moved REF**1006 2.23 mm to (75.2, 101.0)
- moved REF**1007 2.23 mm to (77.7, 101.0)
- moved REF**1008 2.23 mm to (80.3, 101.0)
- moved REF**1009 2.23 mm to (82.8, 101.0)
- moved REF**1010 2.23 mm to (85.3, 101.0)
- moved REF**1011 2.23 mm to (87.9, 101.0)
- moved REF**1012 2.23 mm to (90.4, 101.0)
- moved REF**1013 2.23 mm to (93.0, 101.0)
- moved REF**1014 2.23 mm to (95.5, 101.0)
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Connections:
- J1 pad 10: /D0 -> /A4
- J1 pad 11: /D1 -> /A5
- J1 pad 12: /D2 -> /A6
- J1 pad 13: /D3 -> /A7
- J1 pad 14: /D4 -> /NC14
- J1 pad 15: /D5 -> /NC15
- J1 pad 16: /D6 -> /~{RD}
- J1 pad 17: /D7 -> /~{ROM_CS}
- J1 pad 19: /~{R0M_CS} -> /~{NMI}
- J1 pad 2: /A0 -> /D3
- J1 pad 20: /~{NMI} -> /~{IO_CS}
- J1 pad 21: /~{IO_CS} -> /~{IO_08}
- J1 pad 3: /A1 -> /D2
- J1 pad 33: /~{RAM_CS} -> /NC33
- J1 pad 34: /~{RD} -> /NC34
- J1 pad 36: /NC36 -> /~{RAM_CS}
- J1 pad 38: /NC38 -> /A8
- J1 pad 39: GND -> /A9
- J1 pad 4: /A2 -> /D1
- J1 pad 40: /NC40 -> /A10
- J1 pad 41: /NC41 -> /A11
- J1 pad 42: /A8 -> /A12
- J1 pad 43: /A9 -> /A13
- J1 pad 44: /A10 -> /A14
- J1 pad 45: /A11 -> /A15
- J1 pad 46: /A12 -> /D7
- J1 pad 47: /A13 -> /D6
- J1 pad 48: /A14 -> /D5
- J1 pad 49: /A15 -> /D4
- J1 pad 5: /A3 -> /D0
- J1 pad 6: /A4 -> /A0
- J1 pad 7: /A5 -> /A1
- J1 pad 8: /A6 -> /A2
- J1 pad 9: /A7 -> /A3
- J2 pad 10: /D0 -> /A4
- J2 pad 11: /D1 -> /A5
- J2 pad 12: /D2 -> /A6
- J2 pad 13: /D3 -> /A7
- J2 pad 14: /D4 -> /NC14
- J2 pad 15: /D5 -> /NC15
- J2 pad 16: /D6 -> /~{RD}
- J2 pad 17: /D7 -> /~{ROM_CS}
- J2 pad 19: /~{R0M_CS} -> /~{NMI}
- J2 pad 2: /A0 -> /D3
- J2 pad 20: /~{NMI} -> /~{IO_CS}
- J2 pad 21: /~{IO_CS} -> /~{IO_08}
- J2 pad 3: /A1 -> /D2
- J2 pad 33: /~{RAM_CS} -> /NC33
- J2 pad 34: /~{RD} -> /NC34
- J2 pad 36: /NC36 -> /~{RAM_CS}
- J2 pad 38: /NC38 -> /A8
- J2 pad 39: GND -> /A9
- J2 pad 4: /A2 -> /D1
- J2 pad 40: /NC40 -> /A10
- J2 pad 41: /NC41 -> /A11
- J2 pad 42: /A8 -> /A12
- J2 pad 43: /A9 -> /A13
- J2 pad 44: /A10 -> /A14
- J2 pad 45: /A11 -> /A15
- J2 pad 46: /A12 -> /D7
- J2 pad 47: /A13 -> /D6
- J2 pad 48: /A14 -> /D5
- J2 pad 49: /A15 -> /D4
- J2 pad 5: /A3 -> /D0
- J2 pad 6: /A4 -> /A0
- J2 pad 7: /A5 -> /A1
- J2 pad 8: /A6 -> /A2
- J2 pad 9: /A7 -> /A3
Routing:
- net VCC: track 363.2 -> 389.3 mm
- net GND: track 360.0 -> 378.5 mm, vias 0 -> 1
- net /NC36: track 16.8 -> 0.00 mm
- net /NC34: track 0.00 -> 16.8 mm
- net /NC41: track 16.8 -> 0.00 mm
- net /NC38: track 16.8 -> 0.00 mm
- net /NC33: track 0.00 -> 16.8 mm
- net /NC40: track 16.8 -> 0.00 mm
- net /~{R0M_CS}: track 13.2 -> 0.00 mm
- net /~{IO_08}: track 0.00 -> 13.2 mm
- net /NC14: track 0.00 -> 13.2 mm
- net /~{ROM_CS}: track 0.00 -> 13.2 mm
- net /NC15: track 0.00 -> 13.2 mm
- net /~{RD}: track 16.8 -> 13.2 mm
- net /D7: track 13.2 -> 16.8 mm
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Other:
- board text added: "A10"
- board text added: "A15 A14 A13 A12 A11"
- board text added: "A9 A8 NC"
- board text added: "CLK"
- board text added: "D3 D2 D1 D0 A0 A1 A2 A3 A4 A5 A6 A7 NC"
- board text added: "D4 D5 D6 D7"
- board text added: "GND"
- board text added: "NC NC"
- board text added: "NC ~{RD}"
- board text added: "~{IO_01}"
- board text added: "~{IO_02}"
- board text added: "~{IO_03}"
- board text added: "~{IO_04}"
- board text added: "~{IO_05}"
- board text added: "~{IO_06}"
- board text added: "~{IO_07}"
- board text added: "~{IO_08}"
- board text added: "~{IO_CS}"
- board text added: "~{IRQ}"
- board text added: "~{NMI}"
- board text added: "~{RAM_CS}"
- board text added: "~{RESET}"
- board text added: "~{ROM_CS}"
- board text added: "~{WR}"
- board text removed: "A0 A1 A2 A3 A4 A5 A6 A7"

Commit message: cleanup and minor changes
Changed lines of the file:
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@@
     (effects (font (size 1 0.9) (thickness 0.15)) (justify left bottom))
   )
+  (segment (start 70.1 34.6) (end 72.64 34.6) (width 0.6) (layer "F.Cu") (net 1))
+  (segment (start 120.9 34.6) (end 123.44 34.6) (width 0.6) (layer "F.Cu") (net 1))
+  (segment (start 87.88 34.6) (end 90.42 34.6) (width 0.6) (layer "F.Cu") (net 1))
+  (segment (start 123.44 34.6) (end 125.98 34.6) (width 0.6) (layer "F.Cu") (net 1))
+  (segment (start 82.8 34.6) (end 85.34 34.6) (width 0.6) (layer "F.Cu") (net 1))
   (segment (start 146.3 103.5) (end 146.3 103.49) (width 0.6) (layer "F.Cu") (net 1))
+  (segment (start 65.02 34.6) (end 67.56 34.6) (width 0.6) (layer "F.Cu") (net 1))
   (segment (start 146.3 103.5) (end 143.76 103.5) (width 0.6) (layer "F.Cu") (net 1))
-  (segment (start 148.84 34.6) (end 57.4 34.6) (width 0.6) (layer "F.Cu") (net 1))
   (segment (start 56.32 112.16) (end 54.92 110.76) (width 0.6) (layer "F.Cu") (net 1))
+  (segment (start 143.76 34.6) (end 146.3 34.6) (width 0.6) (layer "F.Cu") (net 1))
+  (segment (start 75.18 34.6) (end 77.72 34.6) (width 0.6) (layer "F.Cu") (net 1))
+  (segment (start 141.22 34.6) (end 143.76 34.6) (width 0.6) (layer "F.Cu") (net 1))
+  (segment (start 92.96 34.6) (end 95.5 34.6) (width 0.6) (layer "F.Cu") (net 1))
+  (segment (start 67.56 34.6) (end 70.1 34.6) (width 0.6) (layer "F.Cu") (net 1))
+  (segment (start 118.36 34.6) (end 120.9 34.6) (width 0.6) (layer "F.Cu") (net 1))
+  (segment (start 128.52 34.6) (end 131.06 34.6) (width 0.6) (layer "F.Cu") (net 1))
+  (segment (start 62.48 34.6) (end 65.02 34.6) (width 0.6) (layer "F.Cu") (net 1))
+  (segment (start 136.14 34.6) (end 138.68 34.6) (width 0.6) (layer "F.Cu") (net 1))
   (segment (start 148.84 95.56) (end 148.84 93.02) (width 0.6) (layer "F.Cu") (net 1))
   (segment (start 54.92 108.2) (end 57.4 105.72) (width 0.6) (layer "F.Cu") (net 1))
+  (segment (start 80.26 34.6) (end 82.8 34.6) (width 0.6) (layer "F.Cu") (net 1))
+  (segment (start 100.58 34.6) (end 103.12 34.6) (width 0.6) (layer "F.Cu") (net 1))
   (segment (start 115.82 103.5) (end 115.82 108.16) (width 0.6) (layer "F.Cu") (net 1))
+  (segment (start 77.72 34.6) (end 80.26 34.6) (width 0.6) (layer "F.Cu") (net 1))
   (segment (start 57.4 34.6) (end 57.4 103.5) (width 0.6) (layer "F.Cu") (net 1))
   (segment (start 148.84 98.1) (end 148.84 95.56) (width 0.6) (layer "F.Cu") (net 1))
   (segment (start 148.84 57.46) (end 148.84 34.6) (width 0.6) (layer "F.Cu") (net 1))
   (segment (start 57.4 103.5) (end 57.4 105.72) (width 0.6) (layer "F.Cu") (net 1))
+  (segment (start 110.74 34.6) (end 113.28 34.6) (width 0.6) (layer "F.Cu") (net 1))
+  (segment (start 95.5 34.6) (end 98.04 34.6) (width 0.6) (layer "F.Cu") (net 1))
+  (segment (start 108.2 34.6) (end 110.74 34.6) (width 0.6) (layer "F.Cu") (net 1))
   (segment (start 62.48 103.5) (end 59.94 103.5) (width 0.6) (layer "F.Cu") (net 1))
   (segment (start 146.3 103.49) (end 148.84 100.95) (width 0.6) (layer "F.Cu") (net 1))
+  (segment (start 59.94 34.6) (end 62.48 34.6) (width 0.6) (layer "F.Cu") (net 1))
   (segment (start 56.32 112.16) (end 56.32 125.38) (width 0.6) (layer "F.Cu") (net 1))
+  (segment (start 113.28 34.6) (end 115.82 34.6) (width 0.6) (layer "F.Cu") (net 1))
+  (segment (start 105.66 34.6) (end 108.2 34.6) (width 0.6) (layer "F.Cu") (net 1))
+  (segment (start 85.34 34.6) (end 87.88 34.6) (width 0.6) (layer "F.Cu") (net 1))
   (segment (start 143.76 103.5) (end 141.22 103.5) (width 0.6) (layer "F.Cu") (net 1))
+  (segment (start 115.82 34.6) (end 118.36 34.6) (width 0.6) (layer "F.Cu") (net 1))
+  (segment (start 125.98 34.6) (end 128.52 34.6) (width 0.6) (layer "F.Cu") (net 1))
   (segment (start 115.82 108.16) (end 117.28 109.62) (width 0.6) (layer "F.Cu") (net 1))
   (segment (start 148.84 87.94) (end 148.84 34.6) (width 0.6) (layer "F.Cu") (net 1))
+  (segment (start 138.68 34.6) (end 141.22 34.6) (width 0.6) (layer "F.Cu") (net 1))
   (segment (start 59.94 103.5) (end 57.4 103.5) (width 0.6) (layer "F.Cu") (net 1))
   (segment (start 148.84 90.48) (end 148.84 87.94) (width 0.6) (layer "F.Cu") (net 1))
+  (segment (start 57.4 34.6) (end 59.94 34.6) (width 0.6) (layer "F.Cu") (net 1))
+  (segment (start 90.42 34.6) (end 92.96 34.6) (width 0.6) (layer "F.Cu") (net 1))
   (segment (start 148.84 93.02) (end 148.84 90.48) (width 0.6) (layer "F.Cu") (net 1))
   (segment (start 148.84 100.95) (end 148.84 98.1) (width 0.6) (layer "F.Cu") (net 1))
   (segment (start 141.22 103.5) (end 62.48 103.5) (width 0.6) (layer "F.Cu") (net 1))
+  (segment (start 98.04 34.6) (end 100.58 34.6) (width 0.6) (layer "F.Cu") (net 1))
+  (segment (start 146.3 34.6) (end 148.84 34.6) (width 0.6) (layer "F.Cu") (net 1))
   (segment (start 54.92 110.76) (end 54.92 108.2) (width 0.6) (layer "F.Cu") (net 1))
+  (segment (start 131.06 34.6) (end 133.6 34.6) (width 0.6) (layer "F.Cu") (net 1))
+  (segment (start 133.6 34.6) (end 136.14 34.6) (width 0.6) (layer "F.Cu") (net 1))
+  (segment (start 103.12 34.6) (end 105.66 34.6) (width 0.6) (layer "F.Cu") (net 1))
+  (segment (start 72.64 34.6) (end 75.18 34.6) (width 0.6) (layer "F.Cu") (net 1))
   (segment (start 56.32 125.38) (end 56.3 125.4) (width 0.25) (layer "F.Cu") (net 1))
   (segment (start 117.28 109.62) (end 118.75 111.09) (width 0.6) (layer "B.Cu") (net 1))

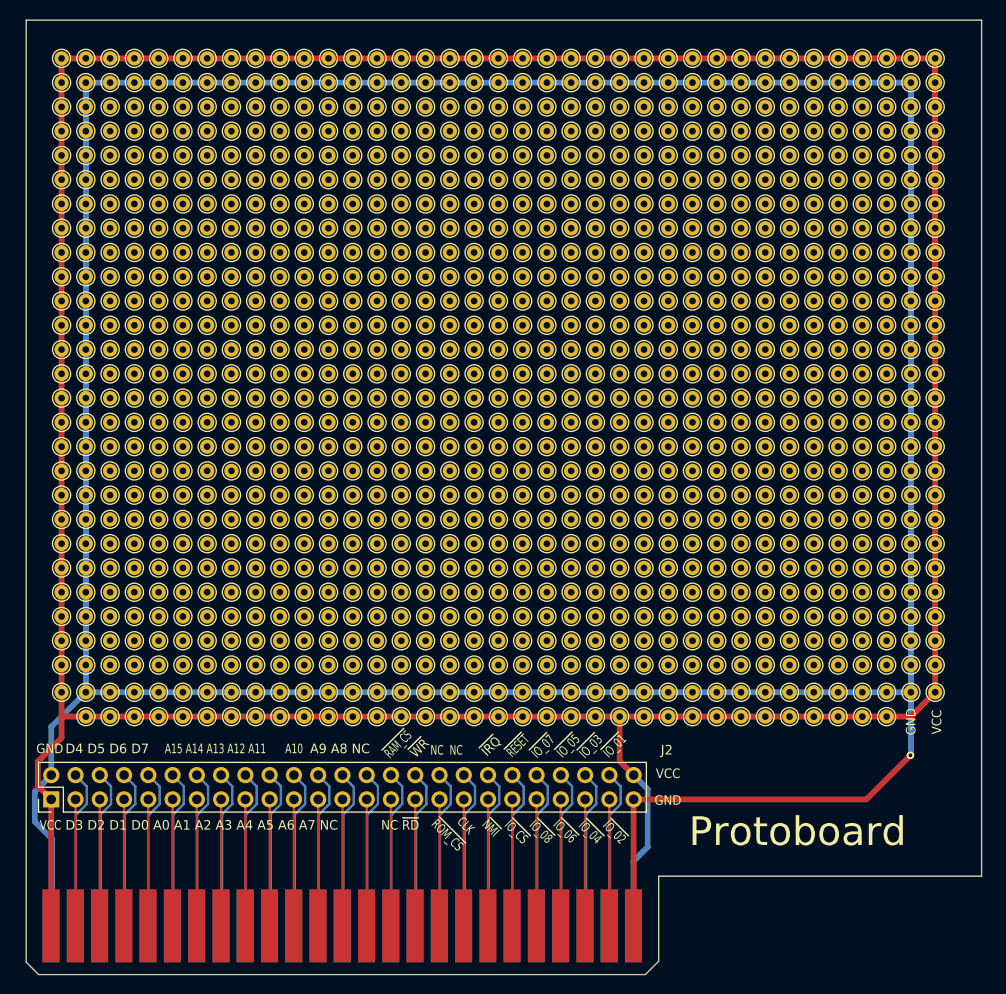
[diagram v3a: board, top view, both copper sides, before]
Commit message: fixed pinout + power led
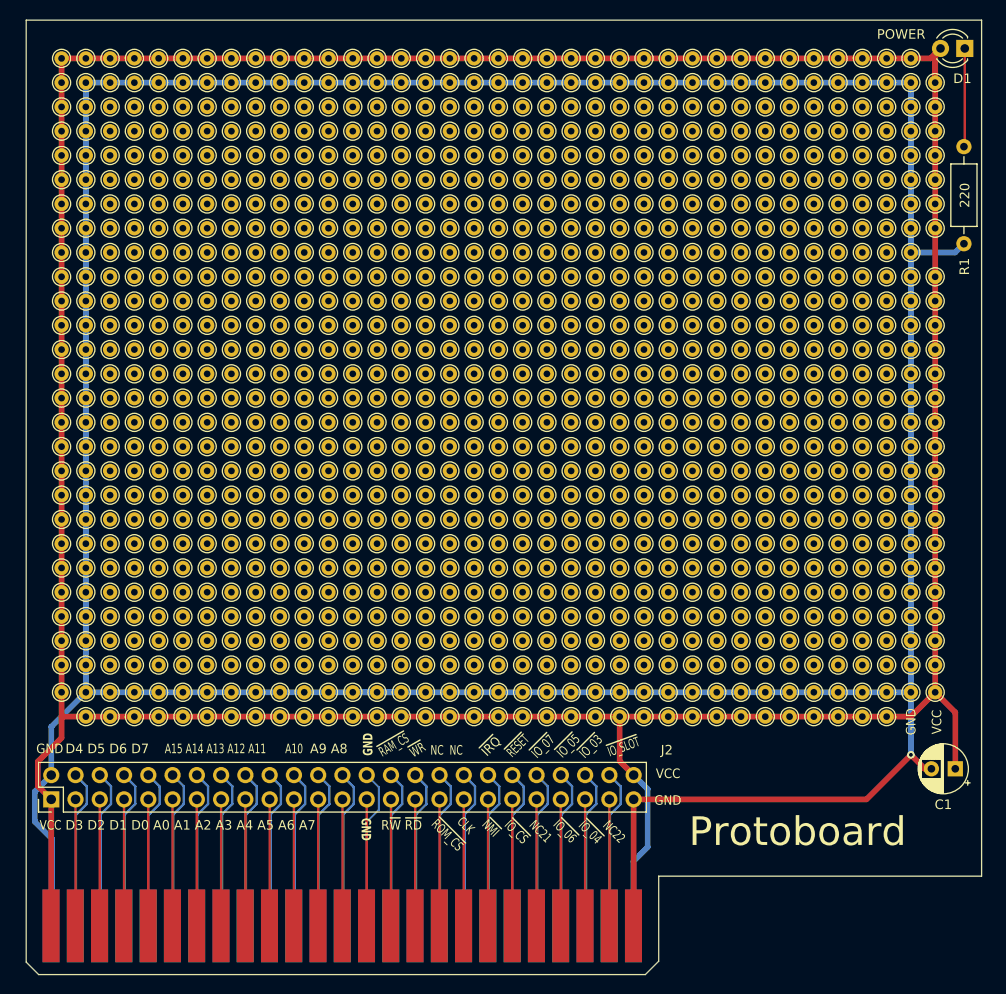
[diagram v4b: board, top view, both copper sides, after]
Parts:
- removed REF**220, REF**36: TestPoint_THTPad_D1.5mm_Drill0.7mm, TestPoint:TestPoint_THTPad_D1.5mm_Drill0.7mm
- added C1: 1000uf, Capacitor_THT:CP_Radial_D5.0mm_P2.50mm, F.Cu at (150.9, 109.0)
- added D1: POWER, LED_THT:LED_D3.0mm, F.Cu at (151.9, 33.6)
- added R1: 220, Resistor_THT:R_Axial_DIN0207_L6.3mm_D2.5mm_P10.16mm_Horizontal, F.Cu at (151.8, 43.8)
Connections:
- net /NC15 renamed /R~{W}
- net /~{IO_01} renamed /~{IO_SLOT}
- net /~{IO_02} renamed /NC24
- net /~{IO_08} renamed /NC21
- J1 pad 14: /NC14 -> GND
- J1 pad 37: /NC37 -> GND
- J2 pad 14: /NC14 -> GND
- J2 pad 37: /NC37 -> GND
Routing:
- net GND: track 378.5 -> 422.4 mm
- net /NC37: track 16.8 -> 0.00 mm
- net /NC14: track 13.2 -> 0.00 mm
- net Net-(D1-K): track 0.00 -> 10.3 mm
- net VCC: track 389.3 -> 380.1 mm
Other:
- board text added: "A9 A8"
- board text added: "D3 D2 D1 D0 A0 A1 A2 A3 A4 A5 A6 A7"
- board text added: "NC21"
- board text added: "NC22"
- board text added: "R~{W} ~{RD}"
- board text added: "~{IO_SLOT}"
- board text removed: "A9 A8 NC"
- board text removed: "D3 D2 D1 D0 A0 A1 A2 A3 A4 A5 A6 A7 NC"
- board text removed: "NC ~{RD}"
- board text removed: "~{IO_01}"
- board text removed: "~{IO_02}"
- board text removed: "~{IO_08}"
